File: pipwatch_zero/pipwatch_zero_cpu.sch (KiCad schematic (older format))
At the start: 1 part, among them U301 STM32F103RXT

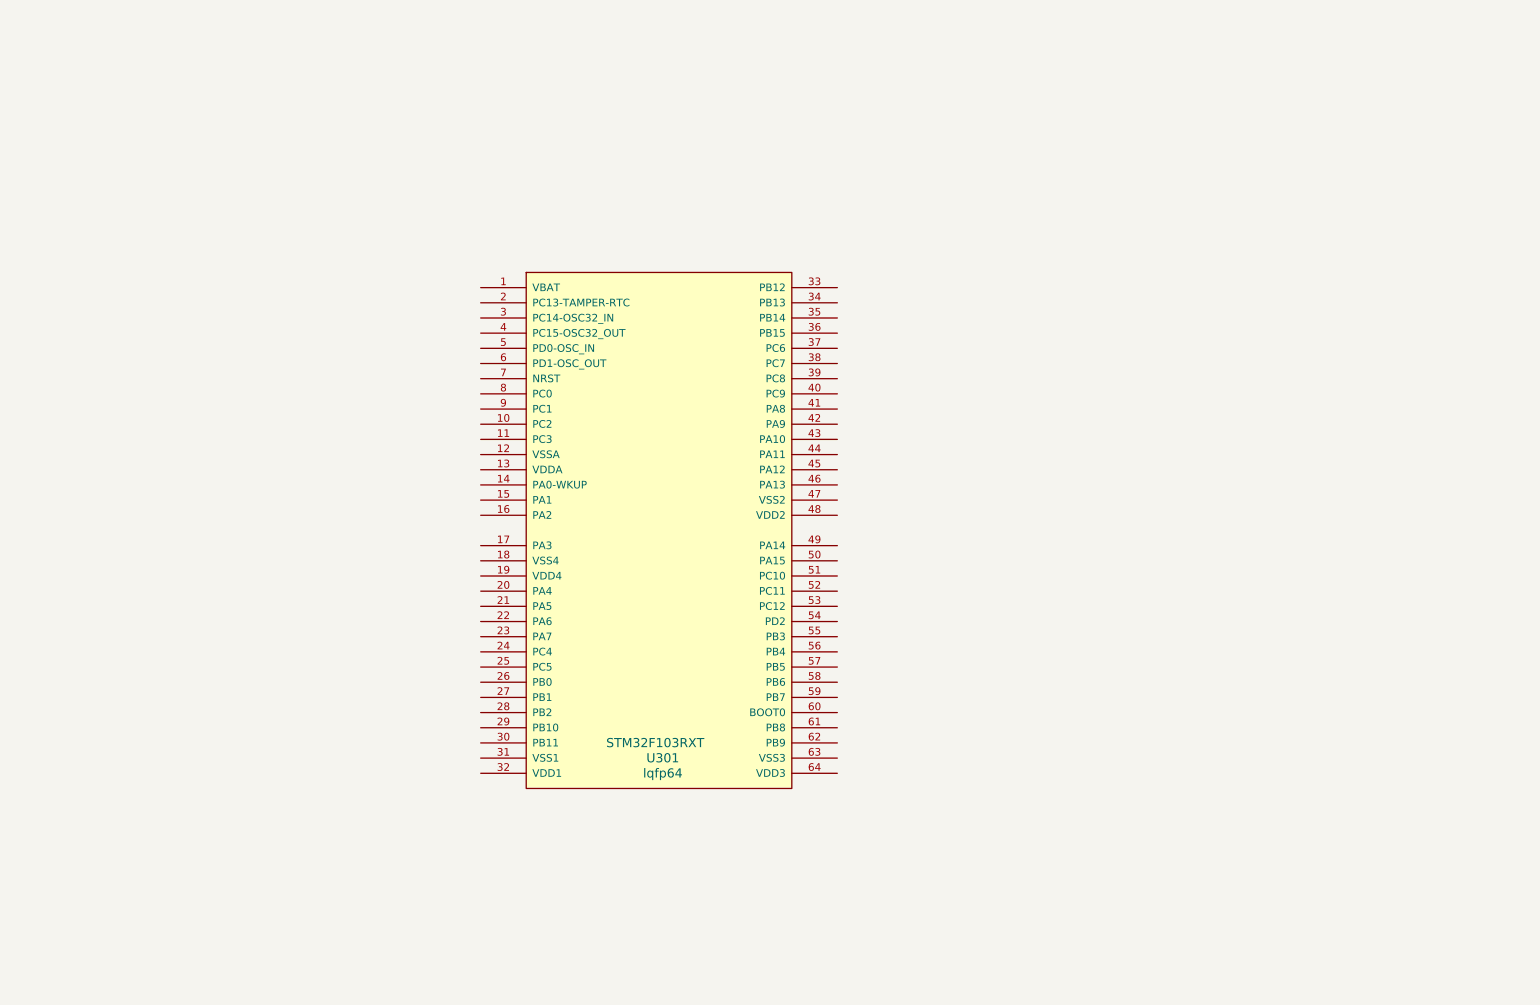
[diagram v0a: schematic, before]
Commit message: hw drawing (started), sw fixes for presentation
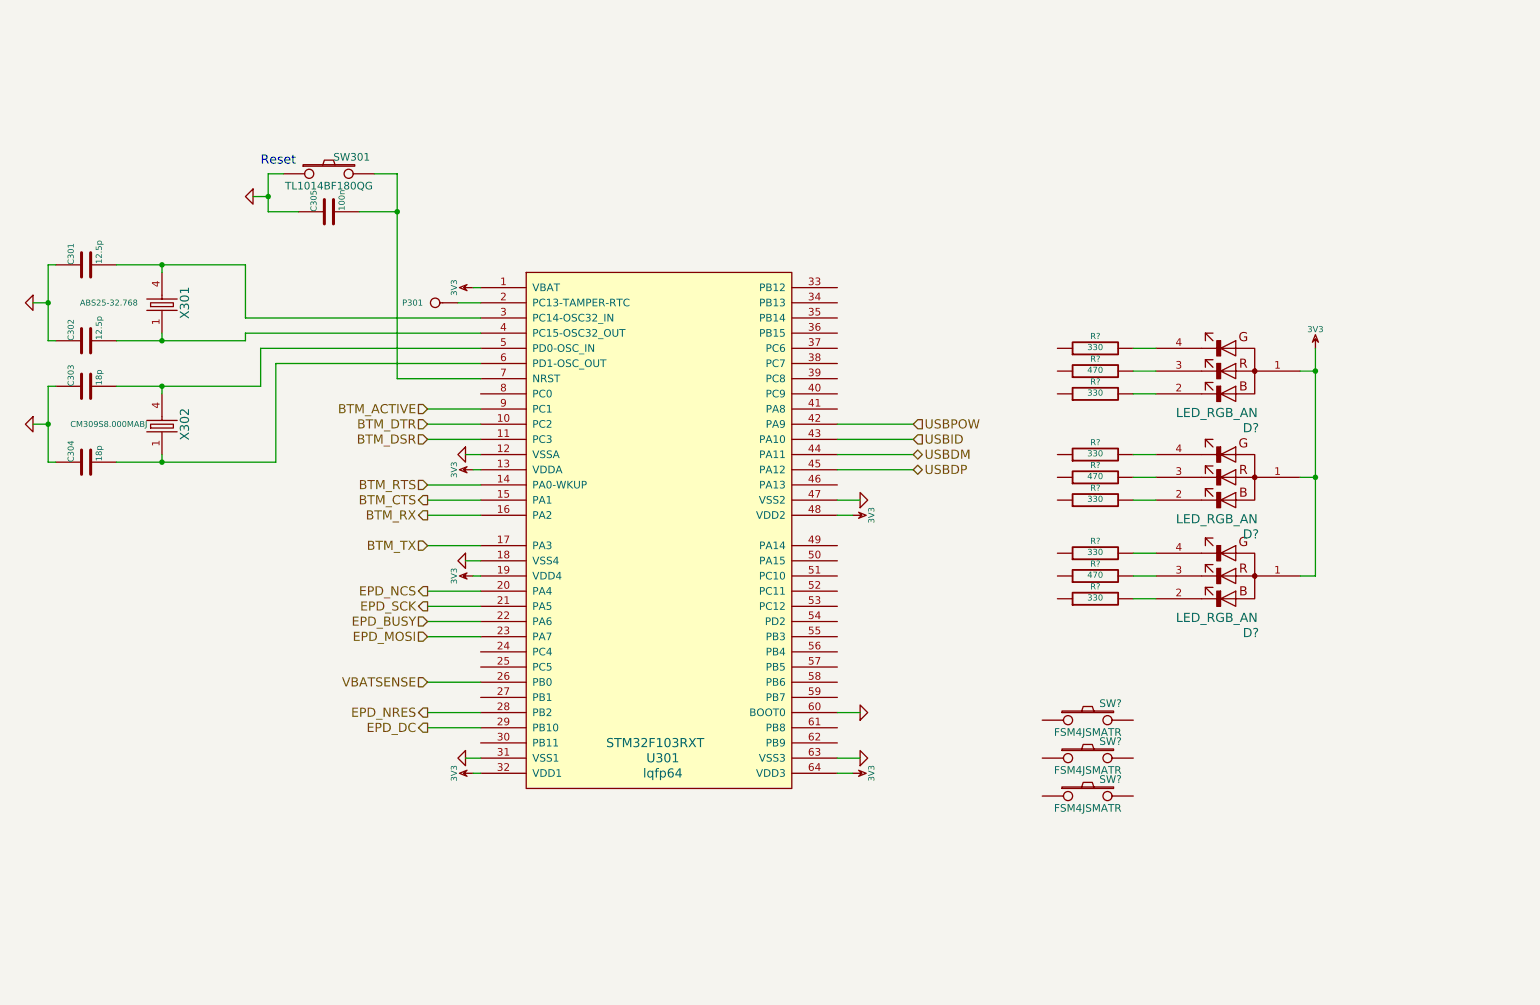
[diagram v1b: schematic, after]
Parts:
- added C301, C302: 12.5p, ~, symbol C
- added C303, C304: 18p, ~, symbol C
- added C305: 100n, ~, symbol C
- added D? (x3): LED_RGB_AN, ~, symbol LED_RGB_AN
- added P301: CONN_1, ~, symbol CONN_1
- added R? (x6): 330, ~, symbol R
- added R? (x3): 470, ~, symbol R
- added SW301: TL1014BF180QG, ~, symbol SW_PUSH
- added SW? (x3): FSM4JSMATR, ~, symbol SW_PUSH
- added X301: ABS25-32.768, symbol XTAL4P
- added X302: CM309S8.000MABJ, symbol XTAL4P
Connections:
- net 3V3: now reaches U301.1 (VBAT)
- net 3V3: now also U301.13 (VDDA), U301.19 (VDD4), U301.32 (VDD1), U301.48 (VDD2), U301.64 (VDD3), D?.1, D?.1, D?.1
- net BTM_DTR: now reaches U301.10 (PC2)
- net BTM_DSR: now reaches U301.11 (PC3)
- net GND: now reaches U301.12 (VSSA)
- net GND: now also U301.18 (VSS4), U301.31 (VSS1), U301.47 (VSS2), U301.60 (BOOT0), U301.63 (VSS3), C301.1, C302.1, C303.1, C304.1, C305.1, SW301.1
- net BTM_RTS: now reaches U301.14 (PA0-WKUP)
- net BTM_CTS: now reaches U301.15 (PA1)
- net BTM_RX: now reaches U301.16 (PA2)
- net BTM_TX: now reaches U301.17 (PA3)
- net at U301.2 (PC13-TAMPER-RTC): now also P301.1
- net EPD_NCS: now reaches U301.20 (PA4)
- net EPD_SCK: now reaches U301.21 (PA5)
- net EPD_BUSY: now reaches U301.22 (PA6)
- net EPD_MOSI: now reaches U301.23 (PA7)
- net VBATSENSE: now reaches U301.26 (PB0)
- net EPD_NRES: now reaches U301.28 (PB2)
- net EPD_DC: now reaches U301.29 (PB10)
- net at U301.3 (PC14-OSC32_IN): now also C301.2, X301.4
- net at U301.4 (PC15-OSC32_OUT): now also C302.2, X301.1
- net USBPOW: now reaches U301.42 (PA9)
- net USBID: now reaches U301.43 (PA10)
- net USBDM: now reaches U301.44 (PA11)
- net USBDP: now reaches U301.45 (PA12)
- net at U301.5 (PD0-OSC_IN): now also C303.2, X302.4
- net at U301.6 (PD1-OSC_OUT): now also C304.2, X302.1
- net at U301.7 (NRST): now also C305.2, SW301.2
- net BTM_ACTIVE: now reaches U301.9 (PC1)
- new net: D?.2, R?.2 (x3)
- new net: D?.3, R?.2 (x3)
- new net: D?.4, R?.2 (x3)
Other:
- note added: "Reset"

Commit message: pipwatch_zero: basic schema complete
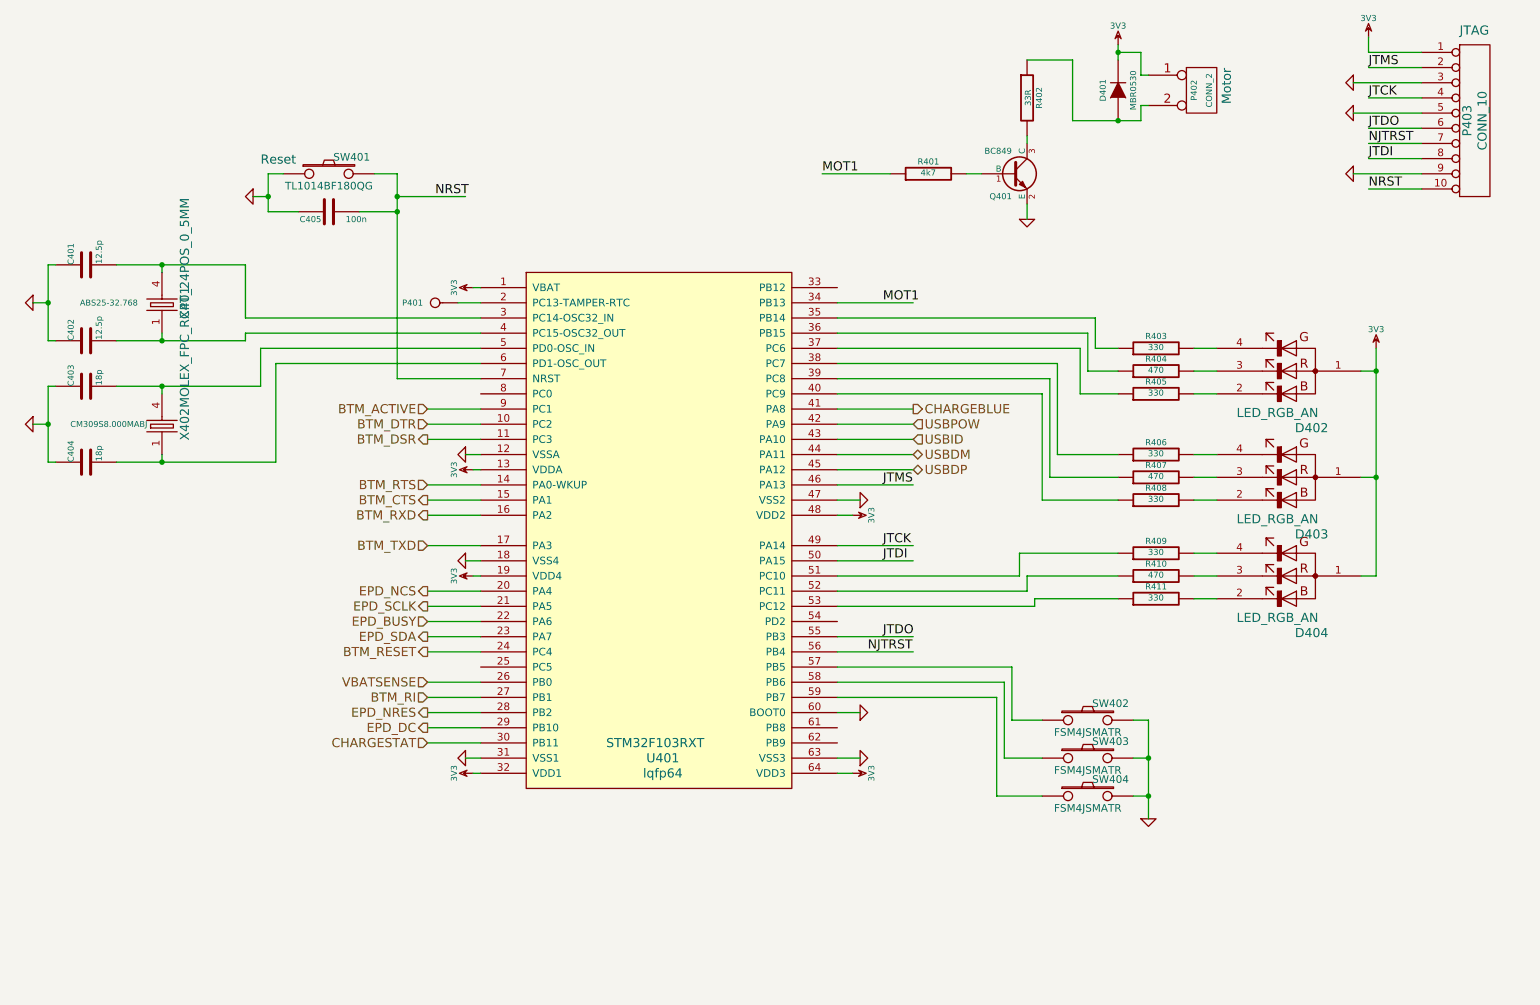
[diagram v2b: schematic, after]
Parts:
- added D401: MBR0530, symbol DIODE
- added P402: CONN_2, symbol CONN_2
- added P403: CONN_10, ~, symbol CONN_10
- added Q401: BC849, symbol BC849
- added R401: 4k7, symbol R
- added R402: 33R, symbol R
- C401: renamed from C301; footprint ~ -> (none)
- C402: renamed from C302; footprint ~ -> (none)
- C403: renamed from C303; footprint ~ -> (none)
- C404: renamed from C304; footprint ~ -> (none)
- C405: renamed from C305; footprint ~ -> (none)
- D402, D403, D404: renamed from D?; footprint ~ -> (none)
- P401: renamed from P301; footprint ~ -> (none)
- R403, R404, R405, R406, R407, R408, R409, R410, R411: renamed from R?; footprint ~ -> (none)
- SW401: renamed from SW301; footprint ~ -> (none)
- SW402, SW403: renamed from SW?; footprint ~ -> (none)
- X401: renamed from X301; footprint (none) -> MOLEX_FPC_RCPT_24POS_0_5MM
- gave numbers to parts that had none: 1
- renumbered U301 to U401, X302 to X402
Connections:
- net labels added: BTM_RESET, BTM_RI, BTM_RXD, BTM_TXD, CHARGEBLUE, CHARGESTAT, EPD_SCLK, EPD_SDA, JTCK, JTDI, JTDO, JTMS, MOT1, NJTRST, NRST
- net labels removed: BTM_RX, BTM_TX, EPD_MOSI, EPD_SCK
- wire segments 76 -> 151
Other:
- note added: "JTAG"
- note added: "Motor"
- moved on the sheet: D402, D403, D404, R403, R404, R405, R406, R407, R408, R409, R410, R411

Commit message: pipwatch_zero: footprints
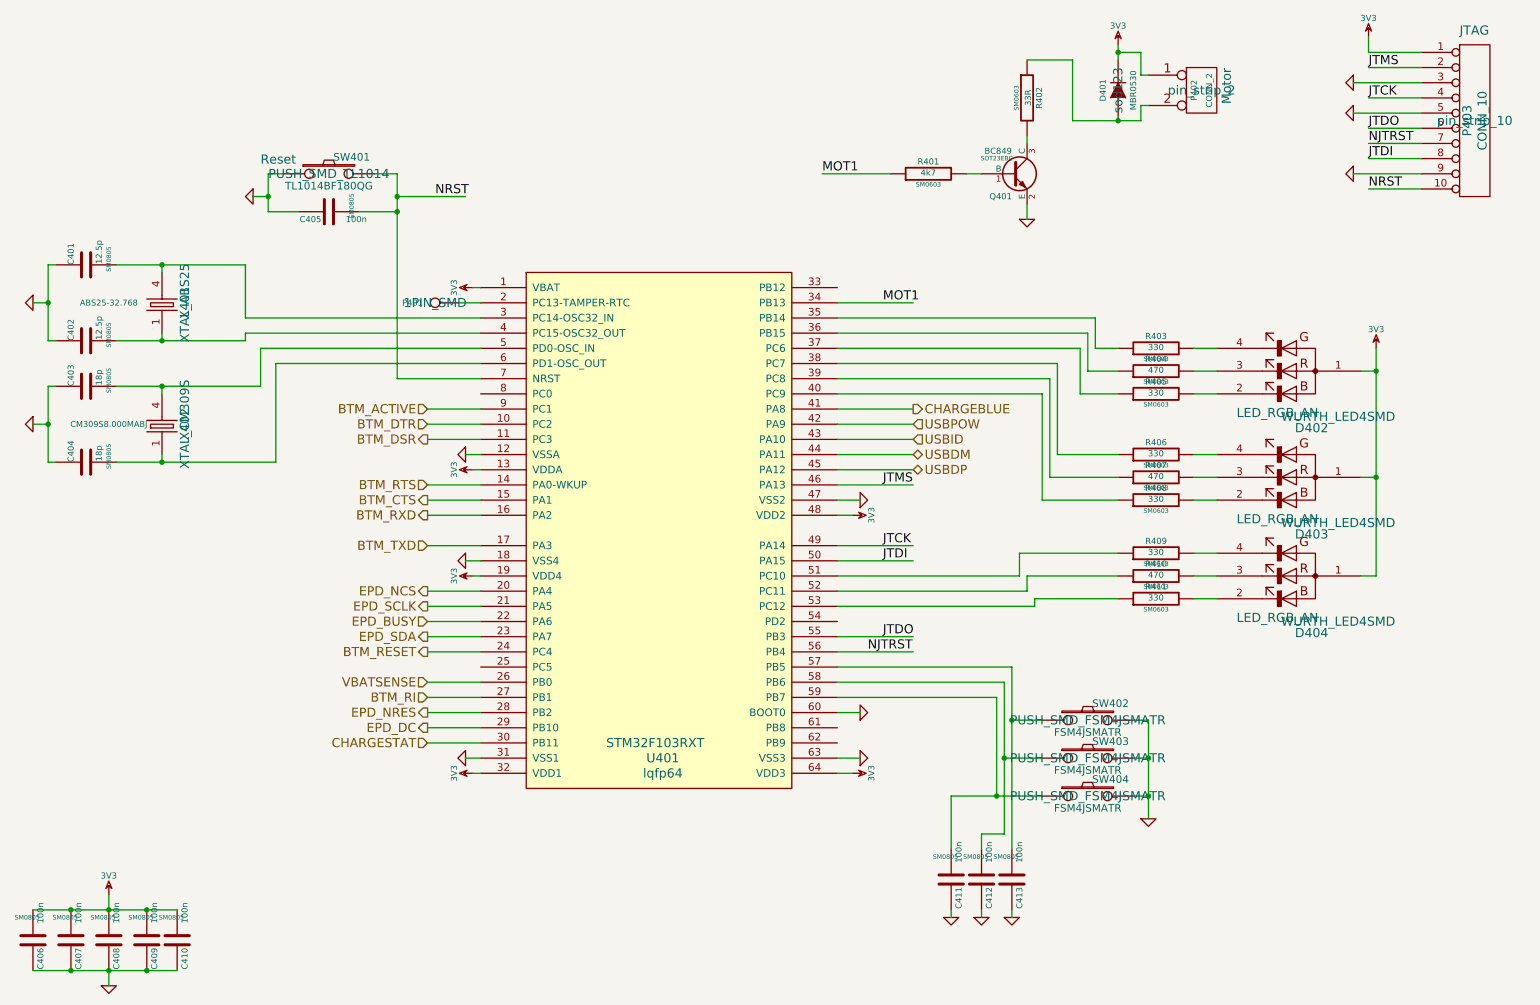
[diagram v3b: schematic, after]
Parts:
- added C406, C407, C408, C409, C410, C411, C412, C413: 100n, SM0805, symbol C
- C401, C402, C403, C404, C405: footprint (none) -> SM0805
- D401: footprint (none) -> sod123
- D402, D403, D404: footprint (none) -> WURTH_LED4SMD
- P401: footprint (none) -> 1PIN_SMD
- P402: footprint (none) -> pin_strip_2
- P403: footprint ~ -> pin_strip_10
- Q401: footprint (none) -> SOT23EBC
- R401, R402, R403, R404, R405, R406, R407, R408, R409, R410, R411: footprint (none) -> SM0603
- SW401: footprint (none) -> PUSH_SMD_TL1014
- SW402, SW403: footprint (none) -> PUSH_SMD_FSM4JSMATR
- SW404: footprint ~ -> PUSH_SMD_FSM4JSMATR
- X401: footprint MOLEX_FPC_RCPT_24POS_0_5MM -> XTAL_ABS25
- X402: footprint (none) -> XTAL_CM309S
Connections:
- wire segments 151 -> 161
